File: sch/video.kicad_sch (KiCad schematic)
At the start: 27 parts, among them X5 DIN-7

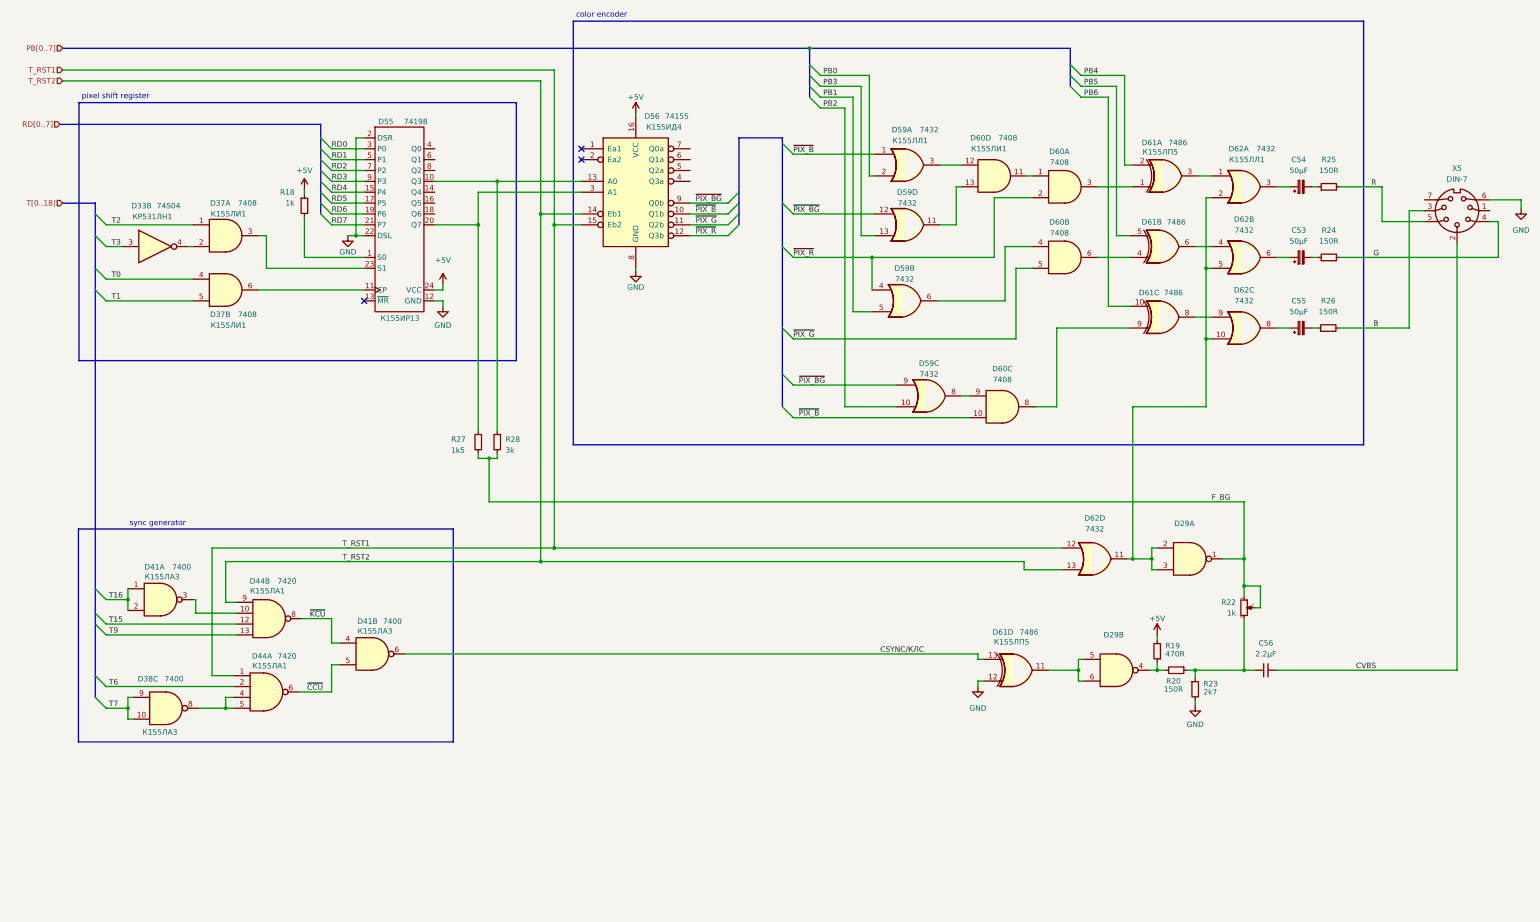
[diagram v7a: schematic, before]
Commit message: Schematics completed with values
Visual corrections pending
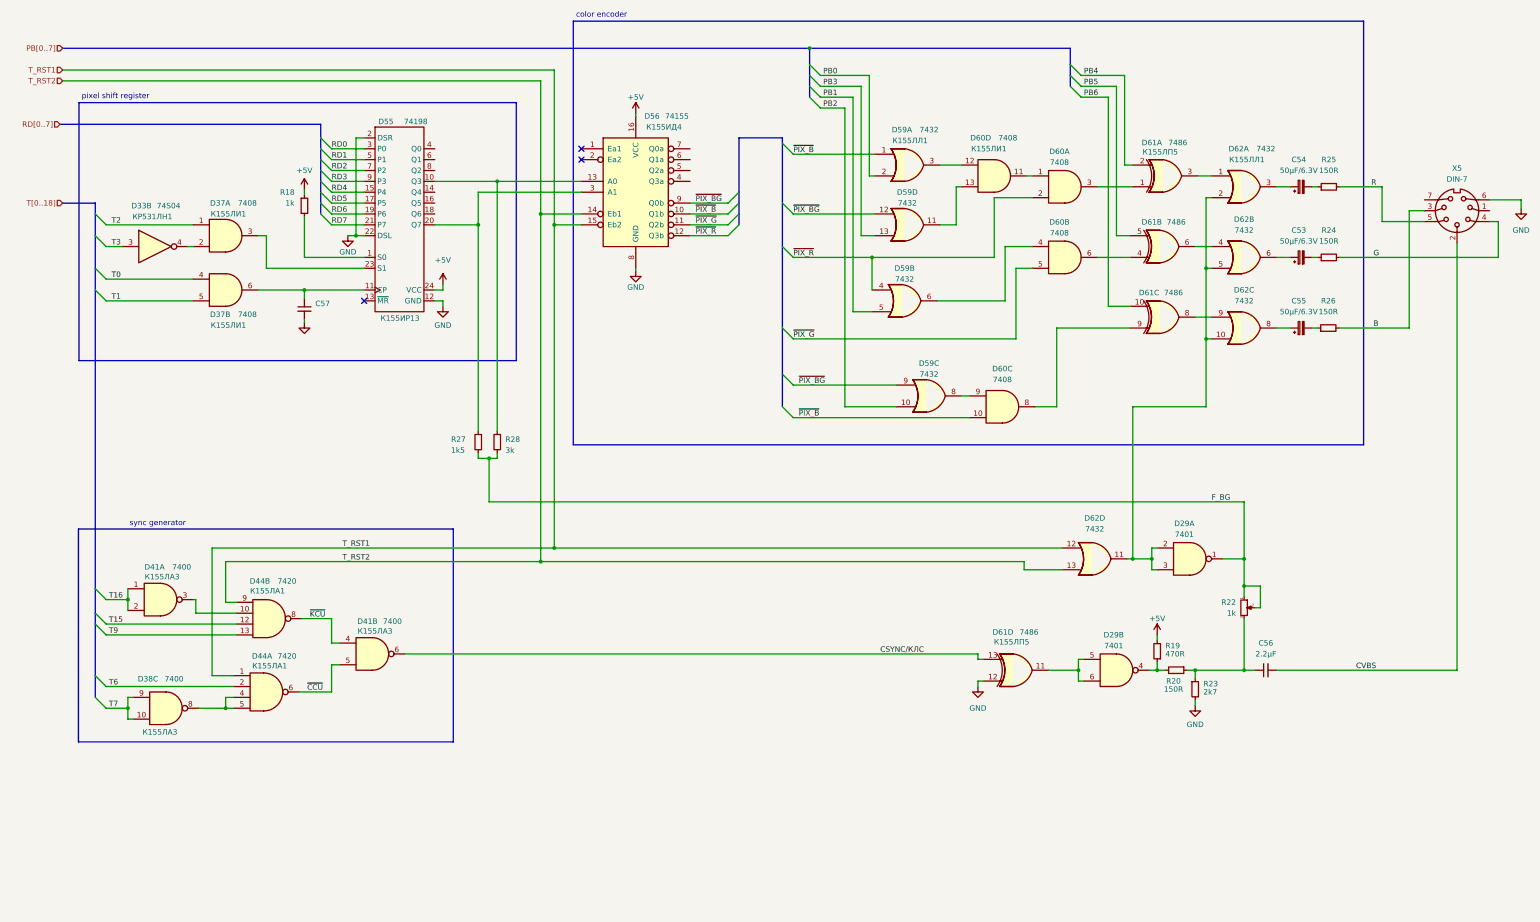
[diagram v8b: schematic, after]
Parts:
- added C57: (no value), symbol Device:C_Small
- C53, C54, C55: value 50μF -> 50μF/6.3V
- D29: value (none) -> 7401; CCCP (none) -> К155ЛА8
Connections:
- net GND: now also C57.2
- net at D37.6, D55.11 (CP): now also C57.1
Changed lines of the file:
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@@
   (junction (at 302.26 83.82) (diameter 0) (color 0 0 0 0)
+  )
+  (junction (at 91.44 88.9) (diameter 0) (color 0 0 0 0)
   )
   (junction (at 302.26 100.33) (diameter 0) (color 0 0 0 0)
@@
     (stroke (width 0) (type default) (color 0 0 0 0))
   )
+  (wire (pts (xy 91.44 95.885) (xy 91.44 96.52))
+    (stroke (width 0) (type default) (color 0 0 0 0))
+  )
   (wire (pts (xy 333.502 81.28) (xy 370.586 81.28))
     (stroke (width 0) (type default) (color 0 0 0 0))
@@
     (stroke (width 0) (type default) (color 0 0 0 0))
   )
-  (wire (pts (xy 80.645 88.9) (xy 105.41 88.9))
+  (wire (pts (xy 80.645 88.9) (xy 91.44 88.9))
     (stroke (width 0) (type default) (color 0 0 0 0))
   )
@@
     (stroke (width 0) (type default) (color 0 0 0 0))
   )
+  (wire (pts (xy 91.44 88.9) (xy 105.41 88.9))
+    (stroke (width 0) (type default) (color 0 0 0 0))
+  )
   (wire (pts (xy 91.44 71.755) (xy 91.44 81.28))
     (stroke (width 0) (type default) (color 0 0 0 0))
   )
   (wire (pts (xy 279.4 92.71) (xy 284.48 92.71))
+    (stroke (width 0) (type default) (color 0 0 0 0))
+  )
+  (wire (pts (xy 91.44 88.9) (xy 91.44 90.805))
     (stroke (width 0) (type default) (color 0 0 0 0))
   )
@@
     (pin "7")
   )
+  (symbol (lib_id "Device:C_Small") (at 91.44 93.345 0) (unit 1)
+    (in_bom yes) (on_board yes) (fields_autoplaced)
+    (property "Reference" "C57" (id 0) (at 93.98 92.0812 0)
+      (effects (font (size 1.27 1.27)) (justify left))
+    )
+    (property "Value" "" (id 1) (at 93.98 94.6212 0)
+      (effects (font (size 1.27 1.27)) (justify left))
+    )
+    (property "Footprint" "" (id 2) (at 91.44 93.345 0)
+      (effects (font (size 1.27 1.27)) hide)
+    )
+    (property "Datasheet" "~" (id 3) (at 91.44 93.345 0)
+      (effects (font (size 1.27 1.27)) hide)
+    )
+    (pin "1")
+    (pin "2")
+  )
   (symbol (lib_id "Device:C_Polarized_Small") (at 324.485 64.77 90) (unit 1)
     (in_bom yes) (on_board yes) (fields_autoplaced)
     (property "Reference" "C54" (id 0) (at 323.9389 58.42 90))
-    (property "Value" "50μF" (id 1) (at 323.9389 60.96 90))
+    (property "Value" "50μF/6.3V" (id 1) (at 323.9389 60.96 90))
     (property "Footprint" "" (id 2) (at 324.485 64.77 0)
       (effects (font (size 1.27 1.27)) hide)
@@
     (in_bom yes) (on_board yes)
     (property "Reference" "D29" (id 0) (at 280.67 169.545 0))
-    (property "Value" "" (id 1) (at 280.67 172.085 0))
+    (property "Value" "7401" (id 1) (at 280.67 172.085 0))
     (property "Footprint" "" (id 2) (at 281.305 177.8 0)
       (effects (font (size 1.27 1.27)) hide)
@@
       (effects (font (size 1.27 1.27)) hide)
     )
+    (property "CCCP" "К155ЛА8" (id 4) (at 281.305 177.8 0)
+      (effects (font (size 1.27 1.27)) hide)
+    )
     (pin "1")
     (pin "2")
@@
     (in_bom yes) (on_board yes)
     (property "Reference" "D29" (id 0) (at 297.18 143.51 0))
-    (property "Value" "" (id 1) (at 297.18 146.05 0))
+    (property "Value" "7401" (id 1) (at 297.18 146.05 0))
     (property "Footprint" "" (id 2) (at 298.45 151.765 0)
       (effects (font (size 1.27 1.27)) hide)
     )
     (property "Datasheet" "http://www.nteinc.com/specs/7400to7499/pdf/nte74LS01.pdf" (id 3) (at 298.45 151.765 0)
+      (effects (font (size 1.27 1.27)) hide)
+    )
+    (property "CCCP" "К155ЛА8" (id 4) (at 298.45 151.765 0)
       (effects (font (size 1.27 1.27)) hide)
     )
@@
     (in_bom yes) (on_board yes) (fields_autoplaced)
     (property "Reference" "C53" (id 0) (at 323.9389 74.93 90))
-    (property "Value" "50μF" (id 1) (at 323.9389 77.47 90))
+    (property "Value" "50μF/6.3V" (id 1) (at 323.9389 77.47 90))
     (property "Footprint" "" (id 2) (at 324.485 81.28 0)
       (effects (font (size 1.27 1.27)) hide)
@@
     (in_bom yes) (on_board yes) (fields_autoplaced)
     (property "Reference" "C55" (id 0) (at 323.9389 91.44 90))
-    (property "Value" "50μF" (id 1) (at 323.9389 93.98 90))
+    (property "Value" "50μF/6.3V" (id 1) (at 323.9389 93.98 90))
     (property "Footprint" "" (id 2) (at 324.485 97.79 0)
       (effects (font (size 1.27 1.27)) hide)
@@
     (pin "7")
   )
+  (symbol (lib_id "power:GND") (at 91.44 96.52 0) (unit 1)
+    (in_bom yes) (on_board yes) (fields_autoplaced)
+    (property "Reference" "#PWR?" (id 0) (at 91.44 102.87 0)
+      (effects (font (size 1.27 1.27)) hide)
+    )
+    (property "Value" "" (id 1) (at 91.44 101.6 0))
+    (property "Footprint" "" (id 2) (at 91.44 96.52 0)
+      (effects (font (size 1.27 1.27)) hide)
+    )
+    (property "Datasheet" "" (id 3) (at 91.44 96.52 0)
+      (effects (font (size 1.27 1.27)) hide)
+    )
+    (pin "1")
+  )
   (symbol (lib_id "74xx:74LS32") (at 231.775 91.44 0) (unit 2)
